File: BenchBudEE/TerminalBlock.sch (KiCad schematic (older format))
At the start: 0 parts

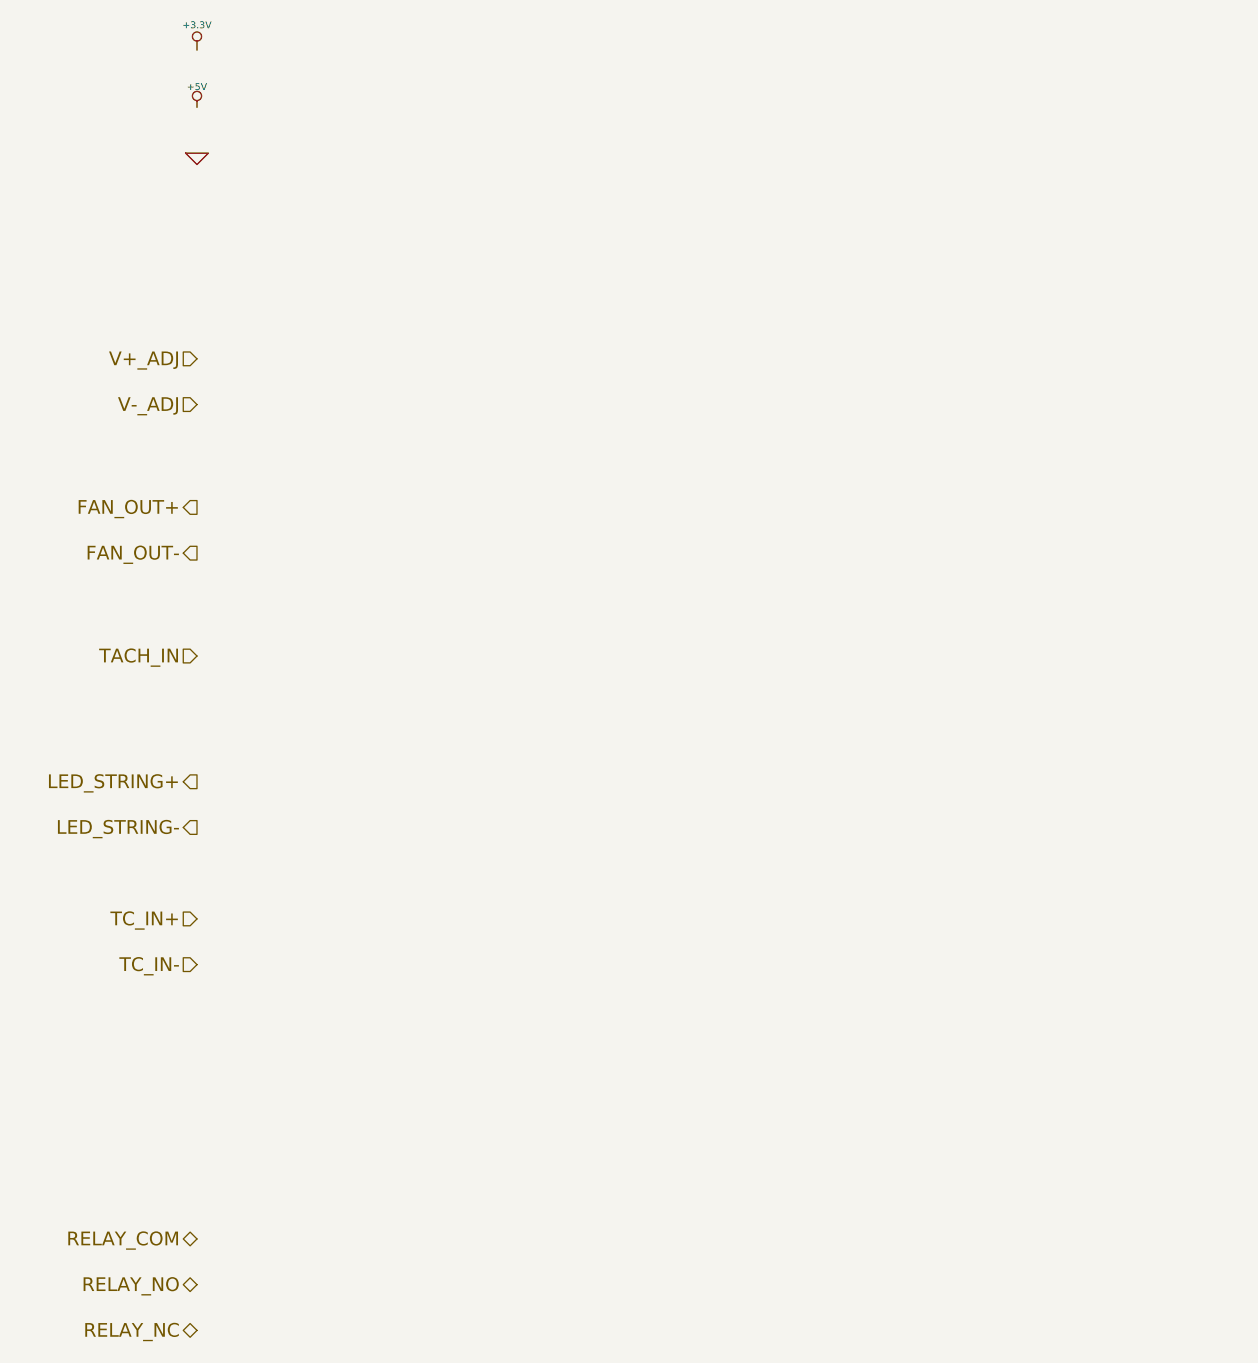
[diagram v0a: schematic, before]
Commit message: Associated the Terminal/ATX block components.
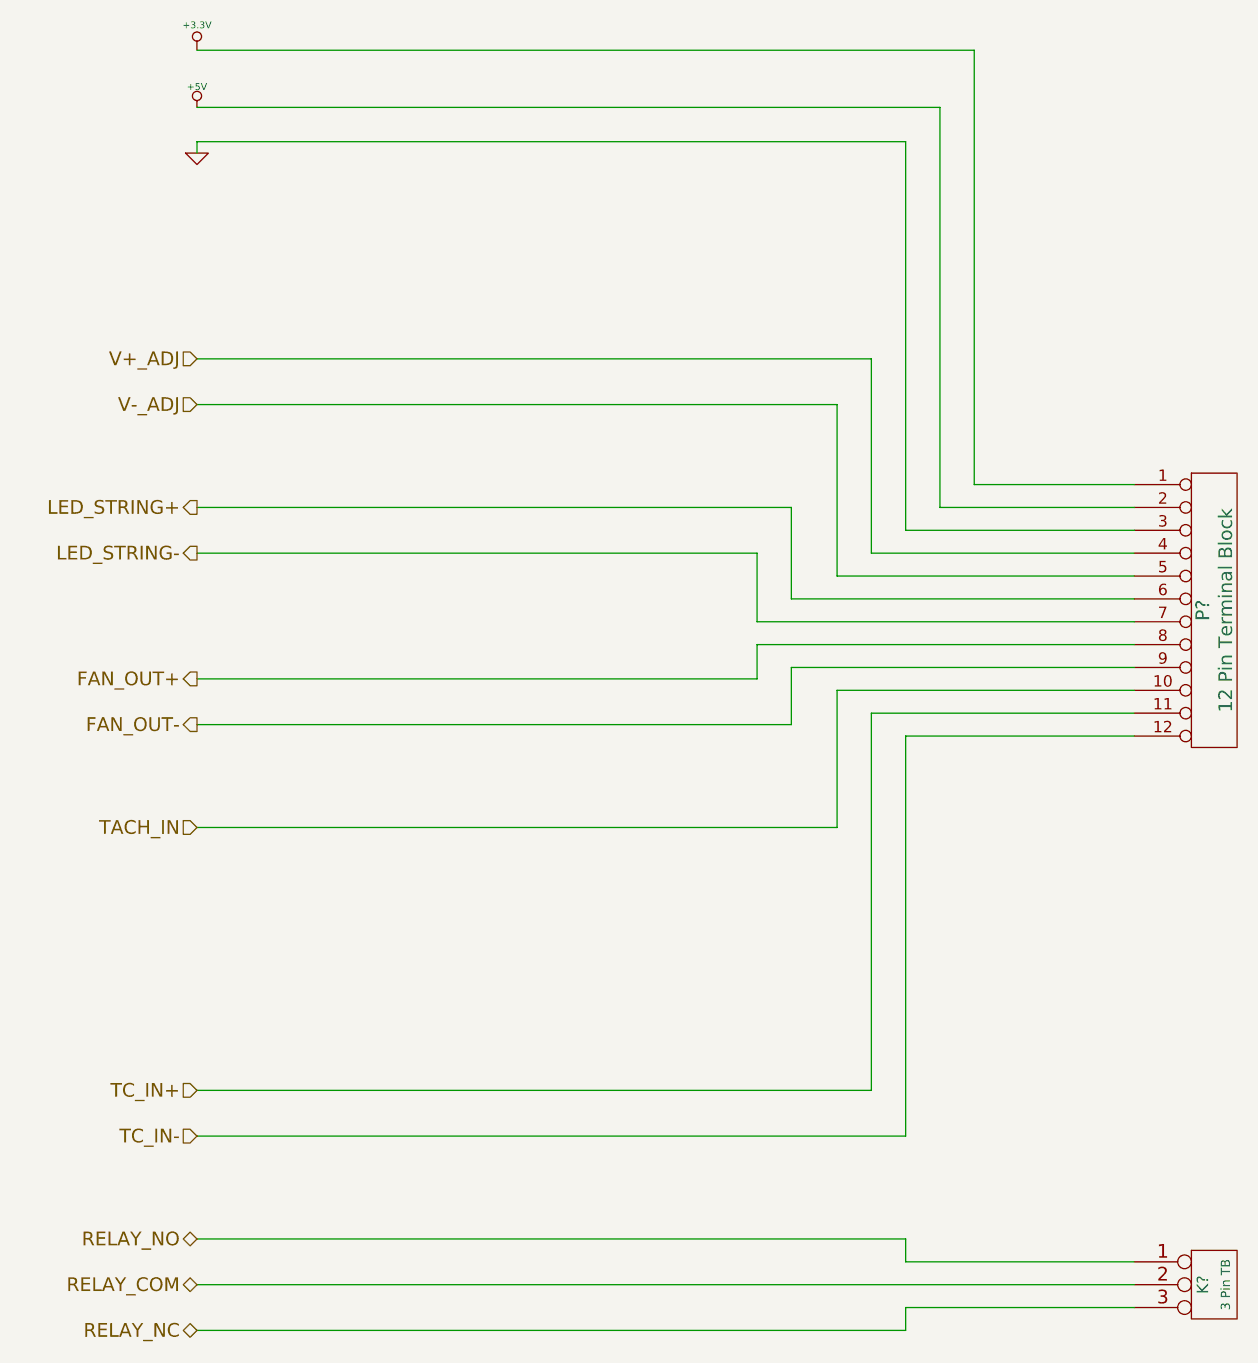
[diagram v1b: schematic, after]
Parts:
- added K?: 3 Pin TB, symbol CONN_3
- added P?: 12 Pin Terminal Block, symbol CONN_12
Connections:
- net +3.3V: now also P?.1 (P1)
- net +5V: now also P?.2 (P2)
- net FAN_OUT+: now also P?.8 (P8)
- net FAN_OUT-: now also P?.9 (P9)
- net GND: now also P?.3 (P3)
- net LED_STRING+: now also P?.6 (P6)
- net LED_STRING-: now also P?.7 (P7)
- net RELAY_COM: now also K?.2 (PM)
- net RELAY_NC: now also K?.3 (P3)
- net RELAY_NO: now also K?.1 (P1)
- net TACH_IN: now also P?.10 (P10)
- net TC_IN+: now also P?.11 (P11)
- net TC_IN-: now also P?.12 (P12)
- net V+_ADJ: now also P?.4 (P4)
- net V-_ADJ: now also P?.5 (P5)
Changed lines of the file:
@@
 $Descr A4 11693 8268
 encoding utf-8
-Sheet 9 9
+Sheet 8 9
 Title ""
-Date "21 feb 2014"
+Date "22 feb 2014"
 Rev ""
 Comp ""
@@
 Text HLabel 1650 3000 0    60   Input ~ 0
 V-_ADJ
+Text HLabel 1650 4200 0    60   Output ~ 0
+FAN_OUT+
+Text HLabel 1650 4400 0    60   Output ~ 0
+FAN_OUT-
+Text HLabel 1650 4850 0    60   Input ~ 0
+TACH_IN
 Text HLabel 1650 3450 0    60   Output ~ 0
-FAN_OUT+
+LED_STRING+
 Text HLabel 1650 3650 0    60   Output ~ 0
-FAN_OUT-
-Text HLabel 1650 4100 0    60   Input ~ 0
-TACH_IN
-Text HLabel 1650 4650 0    60   Output ~ 0
-LED_STRING+
-Text HLabel 1650 4850 0    60   Output ~ 0
 LED_STRING-
-Text HLabel 1650 5250 0    60   Input ~ 0
+Text HLabel 1650 6000 0    60   Input ~ 0
 TC_IN+
-Text HLabel 1650 5450 0    60   Input ~ 0
+Text HLabel 1650 6200 0    60   Input ~ 0
 TC_IN-
+Text HLabel 1650 6850 0    60   BiDi ~ 0
+RELAY_COM
 Text HLabel 1650 6650 0    60   BiDi ~ 0
-RELAY_COM
-Text HLabel 1650 6850 0    60   BiDi ~ 0
 RELAY_NO
 Text HLabel 1650 7050 0    60   BiDi ~ 0
@@
 	1    0    0    -1
 $EndComp
+$Comp
+L CONN_12 P?
+U 1 1 5307F46A
+P 6100 3900
+F 0 "P?" V 6050 3900 60  0000 C CNN
+F 1 "12 Pin Terminal Block" V 6150 3900 60  0000 C CNN
+F 2 "" H 6100 3900 60  0000 C CNN
+F 3 "" H 6100 3900 60  0000 C CNN
+F 4 "On Shore" H 6100 3900 60  0001 C CNN "MFG Name"
+F 5 "OSTTE120104" H 6100 3900 60  0001 C CNN "MFG Part Number"
+	1    6100 3900
+	1    0    0    -1
+$EndComp
+Wire Wire Line
+	5750 3350 5050 3350
+Wire Wire Line
+	5050 3350 5050 1450
+Wire Wire Line
+	5050 1450 1650 1450
+Wire Wire Line
+	5750 3450 4900 3450
+Wire Wire Line
+	4900 3450 4900 1700
+Wire Wire Line
+	4900 1700 1650 1700
+Wire Wire Line
+	5750 3550 4750 3550
+Wire Wire Line
+	4750 3550 4750 1850
+Wire Wire Line
+	4750 1850 1650 1850
+Wire Wire Line
+	1650 1850 1650 1900
+Wire Wire Line
+	5750 3650 4600 3650
+Wire Wire Line
+	4600 3650 4600 2800
+Wire Wire Line
+	4600 2800 1650 2800
+Wire Wire Line
+	5750 3750 4450 3750
+Wire Wire Line
+	4450 3750 4450 3000
+Wire Wire Line
+	4450 3000 1650 3000
+Wire Wire Line
+	5750 3850 4250 3850
+Wire Wire Line
+	4250 3850 4250 3450
+Wire Wire Line
+	4250 3450 1650 3450
+Wire Wire Line
+	5750 3950 4100 3950
+Wire Wire Line
+	4100 3950 4100 3650
+Wire Wire Line
+	4100 3650 1650 3650
+Wire Wire Line
+	5750 4050 4100 4050
+Wire Wire Line
+	4100 4050 4100 4200
+Wire Wire Line
+	4100 4200 1650 4200
+Wire Wire Line
+	5750 4150 4250 4150
+Wire Wire Line
+	4250 4150 4250 4400
+Wire Wire Line
+	4250 4400 1650 4400
+Wire Wire Line
+	5750 4250 4450 4250
+Wire Wire Line
+	4450 4250 4450 4850
+Wire Wire Line
+	4450 4850 1650 4850
+Wire Wire Line
+	5750 4350 4600 4350
+Wire Wire Line
+	4600 4350 4600 6000
+Wire Wire Line
+	4600 6000 1650 6000
+Wire Wire Line
+	5750 4450 4750 4450
+Wire Wire Line
+	4750 4450 4750 6200
+Wire Wire Line
+	4750 6200 1650 6200
+$Comp
+L CONN_3 K?
+U 1 1 5307FD66
+P 6100 6850
+F 0 "K?" V 6050 6850 50  0000 C CNN
+F 1 "3 Pin TB" V 6150 6850 40  0000 C CNN
+F 2 "" H 6100 6850 60  0000 C CNN
+F 3 "" H 6100 6850 60  0000 C CNN
+F 4 "Phoenix Contact" H 6100 6850 60  0001 C CNN "MFG Name"
+F 5 "1935174" H 6100 6850 60  0001 C CNN "MFG Part Number"
+	1    6100 6850
+	1    0    0    -1
+$EndComp
+Wire Wire Line
+	5750 6850 1650 6850
+Wire Wire Line
+	5750 6750 4750 6750
+Wire Wire Line
+	4750 6750 4750 6650
+Wire Wire Line
+	4750 6650 1650 6650
+Wire Wire Line
+	5750 6950 4750 6950
+Wire Wire Line
+	4750 6950 4750 7050
+Wire Wire Line
+	4750 7050 1650 7050
 $EndSCHEMATC

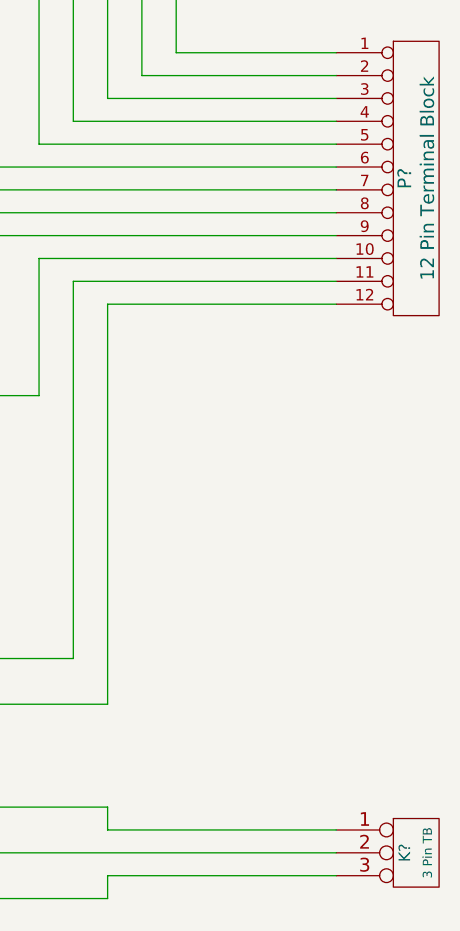
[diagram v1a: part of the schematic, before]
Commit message: Placed the Terminal/ATX block components.
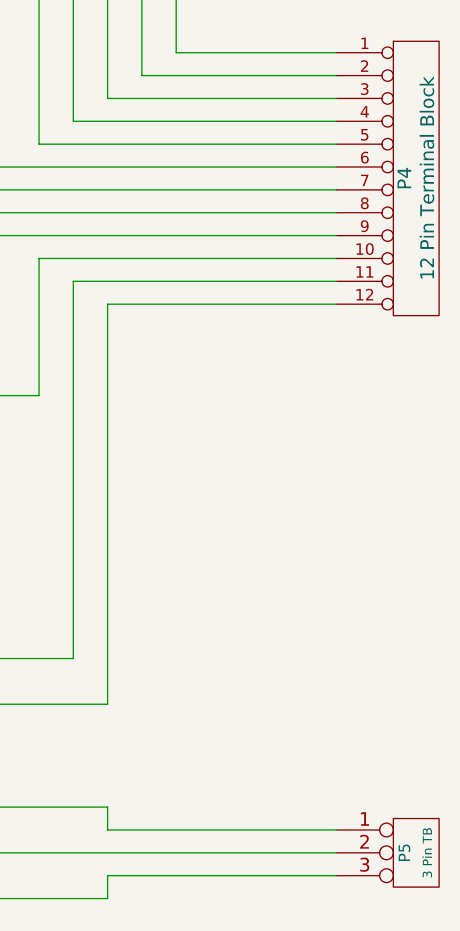
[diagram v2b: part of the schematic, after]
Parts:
- gave numbers to parts that had none: 2
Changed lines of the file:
@@
 RELAY_NC
 $Comp
-L +3.3V #PWR053
+L +3.3V #PWR56
 U 1 1 52F8FA4F
 P 1650 1450
-F 0 "#PWR053" H 1650 1410 30  0001 C CNN
+F 0 "#PWR56" H 1650 1410 30  0001 C CNN
 F 1 "+3.3V" H 1650 1560 30  0000 C CNN
 F 2 "" H 1650 1450 60  0000 C CNN
@@
 $EndComp
 $Comp
-L +5V #PWR054
+L +5V #PWR57
 U 1 1 52F8FA5E
 P 1650 1700
-F 0 "#PWR054" H 1650 1790 20  0001 C CNN
+F 0 "#PWR57" H 1650 1790 20  0001 C CNN
 F 1 "+5V" H 1650 1790 30  0000 C CNN
 F 2 "" H 1650 1700 60  0000 C CNN
@@
 $EndComp
 $Comp
-L GND #PWR055
+L GND #PWR58
 U 1 1 52F8FA6D
 P 1650 1900
-F 0 "#PWR055" H 1650 1900 30  0001 C CNN
+F 0 "#PWR58" H 1650 1900 30  0001 C CNN
 F 1 "GND" H 1650 1830 30  0001 C CNN
 F 2 "" H 1650 1900 60  0000 C CNN
@@
 $EndComp
 $Comp
-L CONN_12 P?
+L CONN_12 P4
 U 1 1 5307F46A
 P 6100 3900
-F 0 "P?" V 6050 3900 60  0000 C CNN
+F 0 "P4" V 6050 3900 60  0000 C CNN
 F 1 "12 Pin Terminal Block" V 6150 3900 60  0000 C CNN
 F 2 "" H 6100 3900 60  0000 C CNN
@@
 	4750 6200 1650 6200
 $Comp
-L CONN_3 K?
+L CONN_3 P5
 U 1 1 5307FD66
 P 6100 6850
-F 0 "K?" V 6050 6850 50  0000 C CNN
+F 0 "P5" V 6050 6850 50  0000 C CNN
 F 1 "3 Pin TB" V 6150 6850 40  0000 C CNN
 F 2 "" H 6100 6850 60  0000 C CNN
